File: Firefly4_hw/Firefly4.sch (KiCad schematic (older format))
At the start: 11 parts

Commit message: sch update, need check
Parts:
- added C? (x8): 0.1u, CAP_0603, symbol C
- added C? (x2): 10u, CAP_0603, symbol C
- added C? (x2): 20pF, CAP_0603, symbol C
- added DD?: STM32L151CxTx, symbol STM32L151CxTx
- added Q?: ALS-PT19-315C, symbol Phototransistor
- added Q?: LED_RGB, symbol LED_RGB
- added Q? (x3): LED_RGB_WS2812B, symbol LED_RGB_WS2812B
- added R?: 200R, RES_0603, symbol R
- added R?: 10k, RES_0603, symbol R
- added R? (x3): 51R, RES_0603, symbol R
- added XL?: ST_SWD, symbol ST_SWD
- added XL?: CONN_3, symbol CONN_3
- added XL?: USB_AM_PCB, symbol USB_AM_PCB
- added XTAL?: 12MHz, CRYSTAL, symbol CRYSTAL_H
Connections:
- net +3.3V: now also C?.1, C?.1, C?.1, C?.1, C?.1, C?.1, DD?.1 (VDD), DD?.24 (VDD1), DD?.36 (VDD2), DD?.48 (VDD3), DD?.9 (VDDA), Q?.1 (C), XL?.1 (Vdd)
- net GND: now also C?.2, C?.2, C?.2, C?.2, C?.2, C?.2, C?.2, C?.2, C?.2, C?.2, C?.2, C?.2, DD?.23 (VSS1), DD?.35 (VSS2), DD?.44 (BOOT0), DD?.47 (VSS3), DD?.8 (VSSA), Q?.3 (GND), Q?.3 (GND), Q?.3 (GND), Q?.BC (B), Q?.GC (G), Q?.RC, R?.2, XL?.1 (P1), XL?.3 (GND), XTAL?.H
- new net: C?.1, DD?.11 (ADC1/T2C2/PA1), Q?.2 (E), R?.1
- new net: C?.1, DD?.5 (OSCIN/PH0), XTAL?.2
- new net: DD?.6 (OSCOUT/PH1), R?.2
- new net: C?.1, R?.1, XTAL?.1
- new net: Q?.BA, R?.1
- new net: Q?.GA, R?.1
- new net: Q?.RA, R?.1
- new net: C?.1, Q?.1 (VDD) (x3)
- new net: Q?.2 (DOUT), Q?.4 (DIN) (x2)
- new net D+: DD?.33 (MOSI1/USBDP/PA12), XL?.3 (D+)
- new net D-: DD?.32 (MISO1/USBDM/PA11), XL?.2 (D-)
- new net DINO: DD?.19 (PB1/T3C4/ADC9), Q?.4 (DIN)
- new net LED_B: DD?.18 (PB0/T3C3/ADC8), R?.2
- new net LED_G: DD?.17 (ADC7/T11C1/T3C2/MOSI1/PA7), R?.2
- new net LED_R: DD?.16 (ADC6/T10C1/T3C1/MISO1/PA6), R?.2
- new net SWCLK: DD?.37 (SWCLK/JTCK/PA14), XL?.2 (SWCLK)
- new net SWDIO: DD?.34 (SWDIO/JTMS/PA13), XL?.4 (SWDIO)
- new net UART_RX: DD?.31 (RX1/PA10), XL?.3
- new net UART_TX: DD?.30 (TX1/PA9), XL?.2 (PM)
- no-connect marks 1 -> 2

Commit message: Sch seems completed
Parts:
- removed F?: Fuse0R, symbol Fuse0R
- removed SW?: SWITCH, symbol SWITCH
- added C?: 1u, symbol C
- added C?: 0.1u, CAP_0603, symbol C
- added C?: 10u, CAP_0603, symbol C
- added DA?: NCP583SQ, ~, symbol NCP583SQ
- added SW?: BUTTON, symbol BUTTON
- added TP?: TESTPOINT, symbol TESTPOINT
- added XL?: CONN_4, symbol CONN_4
- added XL?: CONN_5, symbol CONN_5
- L?: footprint IND_0402 -> IND_1810
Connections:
- net BAT_IN is gone; now on net +BATT: XL?.1 (P1)
- net +3.3V: now also DA?.2 (OUT), C?.1, DA?.3 (Vout), SW?.2; no longer DA?.3 (NC)
- net D+: now also XL?.3
- net D-: now also XL?.2 (PM)
- net GND: now also XL?.4 (UGND), C?.2, C?.2, C?.2, DA?.2 (GND), XL?.4, XL?.5
- net at DD?.10 (ADC0/T2C1ETR/WKUP/PA0): now also SW?.1
- net at DD?.12 (ADC2/T9C1/T2C3/TX2/PA2): now also XL?.1
- net at DD?.13 (ADC3/T9C2/T2C4/RX2/PA3): now also XL?.2
- net at DD?.14 (ADC4/DAC1/CK2/PA4): now also XL?.3
- net at DD?.7 (NRST): now also TP?.1
- net +5V: now reaches C?.1, Q?.1 (VDD)
- net +5V: now also C?.1, C?.1, Q?.1 (VDD), Q?.1 (VDD), XL?.1 (UVcc), C?.1, C?.1, DA?.1 (EN), DA?.4 (Vin), XL?.1 (P1), XL?.4
- no-connect marks 2 -> 7
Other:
- moved on the sheet: C?, Q?, R?, XL?

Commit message: sch update
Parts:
- C12, C13, C2, C3, C8: renamed from C?; footprint CAP_0603 -> CAP_0805
- C9: renamed from C?; footprint (none) -> CAP_0603
- gave numbers to parts that had none: 38
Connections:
- no-connect marks 7 -> 21
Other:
- moved on the sheet: C1, C11, C12, C2, C4, C9, D1, DA1, DA2, L1, XL5, XL6

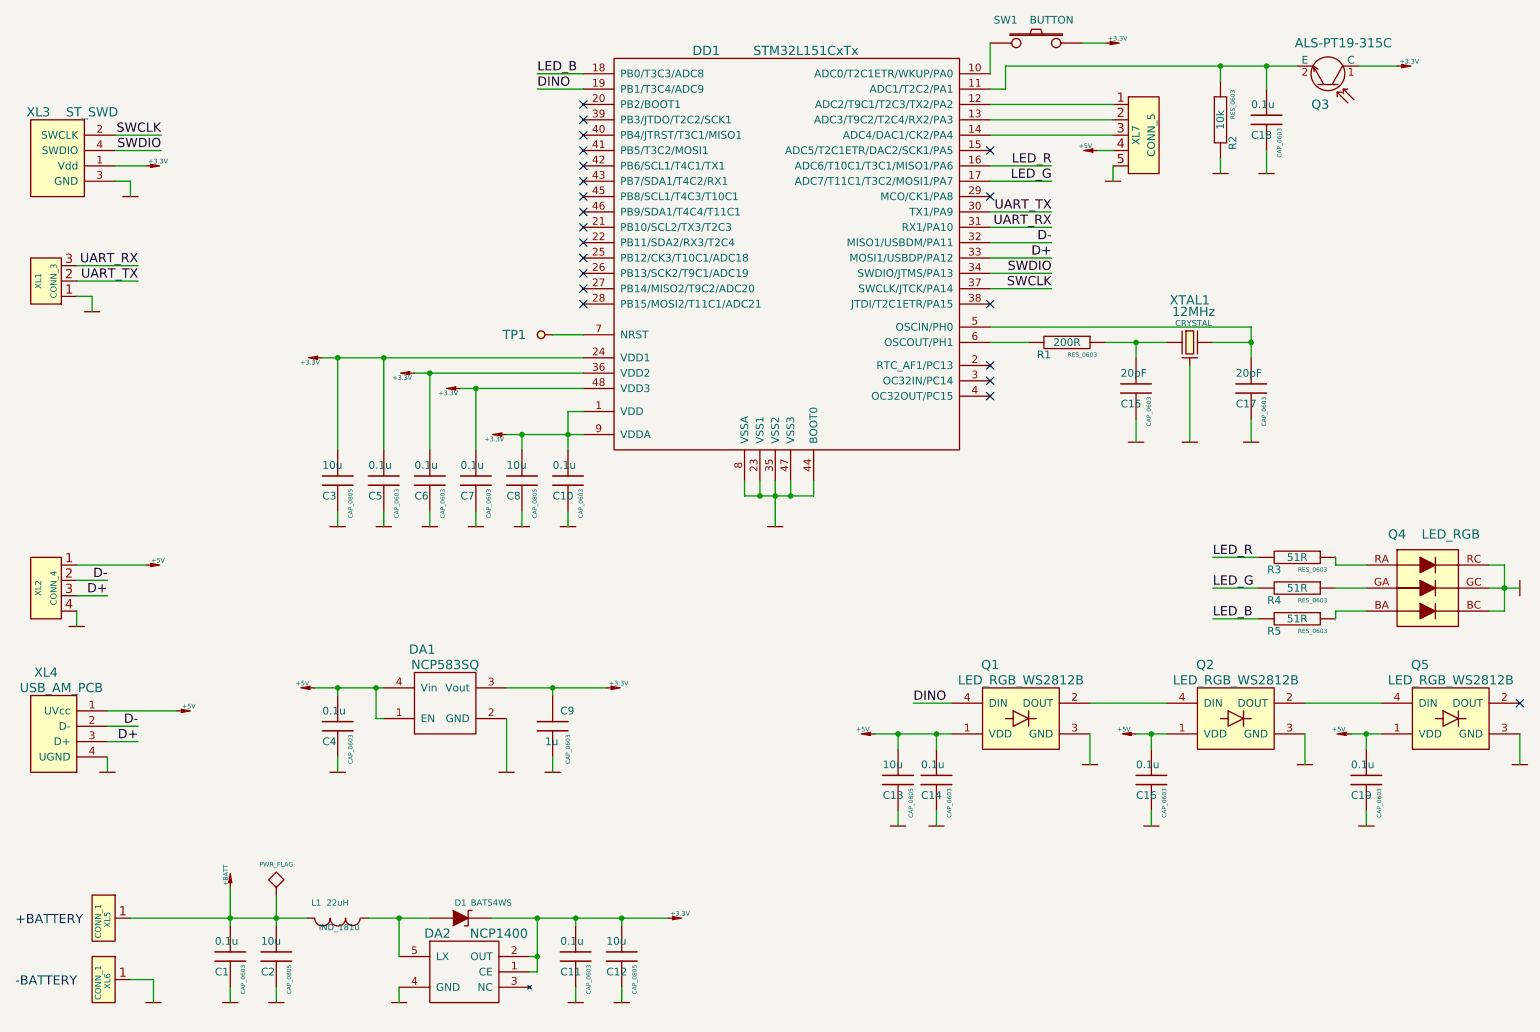
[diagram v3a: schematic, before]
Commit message: + LDO & Booster control
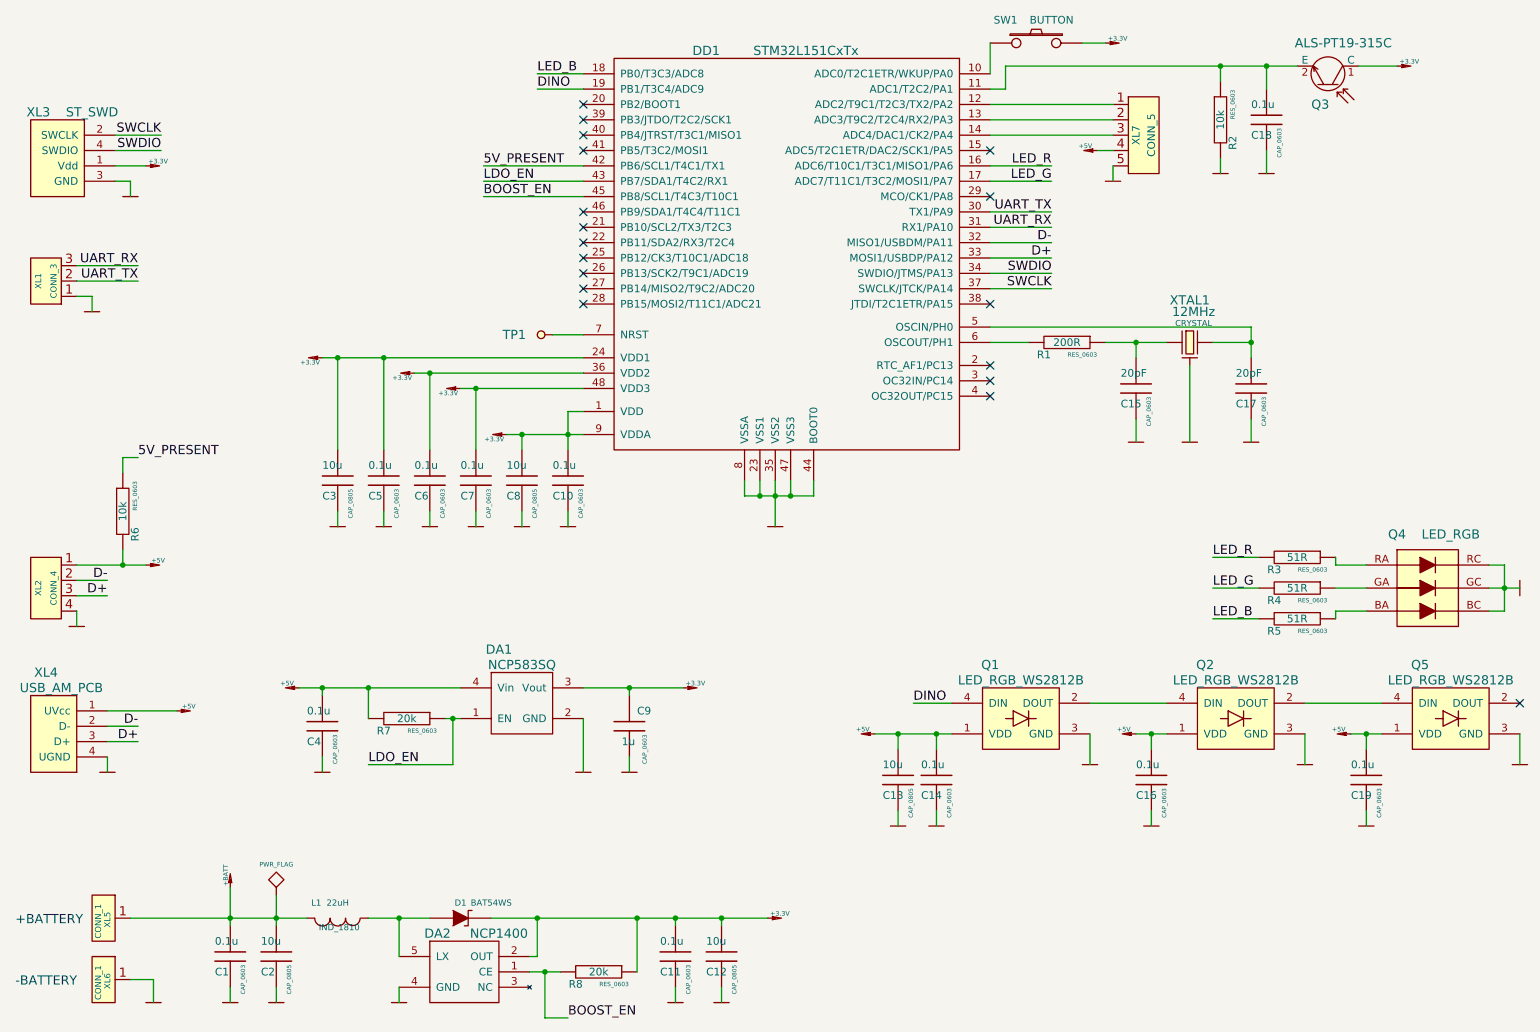
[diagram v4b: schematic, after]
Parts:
- added R6: 10k, RES_0603, symbol R
- added R7, R8: 20k, RES_0603, symbol R
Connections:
- net +3.3V: now also R8.1; no longer DA2.1 (CE)
- net +5V: now also R6.2, R7.2; no longer DA1.1 (EN)
- net 5V_PRESENT: now reaches DD1.42 (PB6/SCL1/T4C1/TX1)
- net 5V_PRESENT: now also R6.1
- net LDO_EN: now reaches DD1.43 (PB7/SDA1/T4C2/RX1)
- net LDO_EN: now also DA1.1 (EN), R7.1
- net BOOST_EN: now reaches DD1.45 (PB8/SCL1/T4C3/T10C1)
- net BOOST_EN: now also DA2.1 (CE), R8.2
- no-connect marks 21 -> 18
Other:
- moved on the sheet: C11, C12, C4, C9, DA1

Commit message: + CvPcb
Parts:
- removed XL5, XL6: CONN_1, symbol CONN_1
- added B1: BAT, Batteries_kl:BATTERY_AA_X1, symbol BAT
- C1, C10, C11, C14, C15, C16, C17, C18, C19, C4, C5, C6, C7, C9: footprint CAP_0603 -> Capacitors:CAP_0603
- C12, C13, C2, C3, C8: footprint CAP_0805 -> Capacitors:CAP_0805
- D1: footprint (none) -> Diodes:SOD323
- DA1: footprint ~ -> SOT:SC82AB
- DA2: footprint (none) -> SOT:SOT23-5
- DD1: footprint (none) -> LQFP_TQFP:LQFP48
- L1: footprint IND_1810 -> Inductors:IND_1210_LQH32C
- Q1, Q2, Q5: footprint (none) -> LEDs:LED_WS2812B
- Q3: footprint (none) -> Resistors:RES_0603
- Q4: footprint (none) -> LEDs:LED_5050
- R1, R2, R3, R4, R5, R6, R7, R8: footprint RES_0603 -> Resistors:RES_0603
- SW1: footprint (none) -> BtnsSwitches:BTN_4x4_SMD
- TP1: footprint (none) -> PCB:TESTPOINT_1MM
- XL1: footprint (none) -> Connectors:PLS-3
- XL2, XL3: footprint (none) -> Connectors:PLS-4
- XL4: footprint (none) -> Connectors:USB_AM_PCB
- XL7: footprint (none) -> Connectors:PLS-5
- XTAL1: footprint CRYSTAL -> Quartz:0503x4-4
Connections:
- net +BATT: now also B1.A
- net GND: now also B1.C
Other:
- note removed: "+BATTERY"
- note removed: "-BATTERY"

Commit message: pcb done  + gerber
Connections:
- net LED_B: now also DD1.16 (ADC6/T10C1/T3C1/MISO1/PA6); no longer DD1.18 (PB0/T3C3/ADC8)
- net LED_G: now also DD1.18 (PB0/T3C3/ADC8); no longer DD1.17 (ADC7/T11C1/T3C2/MOSI1/PA7)
- net LED_R: now also DD1.17 (ADC7/T11C1/T3C2/MOSI1/PA7); no longer DD1.16 (ADC6/T10C1/T3C1/MISO1/PA6)
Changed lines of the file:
@@
 Text Label 8900 4750 0    60   ~ 0
 LED_B
+Text Label 7850 1900 2    60   ~ 0
+LED_R
+Text Label 4500 1200 0    60   ~ 0
+LED_G
 Text Label 7850 1800 2    60   ~ 0
-LED_R
-Text Label 7850 1900 2    60   ~ 0
-LED_G
-Text Label 4500 1200 0    60   ~ 0
 LED_B
 Text Label 4500 1300 0    60   ~ 0
